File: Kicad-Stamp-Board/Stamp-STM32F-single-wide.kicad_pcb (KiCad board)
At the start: 2 copper layers, 70 x 84 mm, 70 parts, among them J1 +3.3V, J2 GND, J3 Serial, J4 BOOT1, SW1 Reset, SW2 BOOT, U1 STM32Fxxx, U2 ICL3221, Y1 32.768KHz

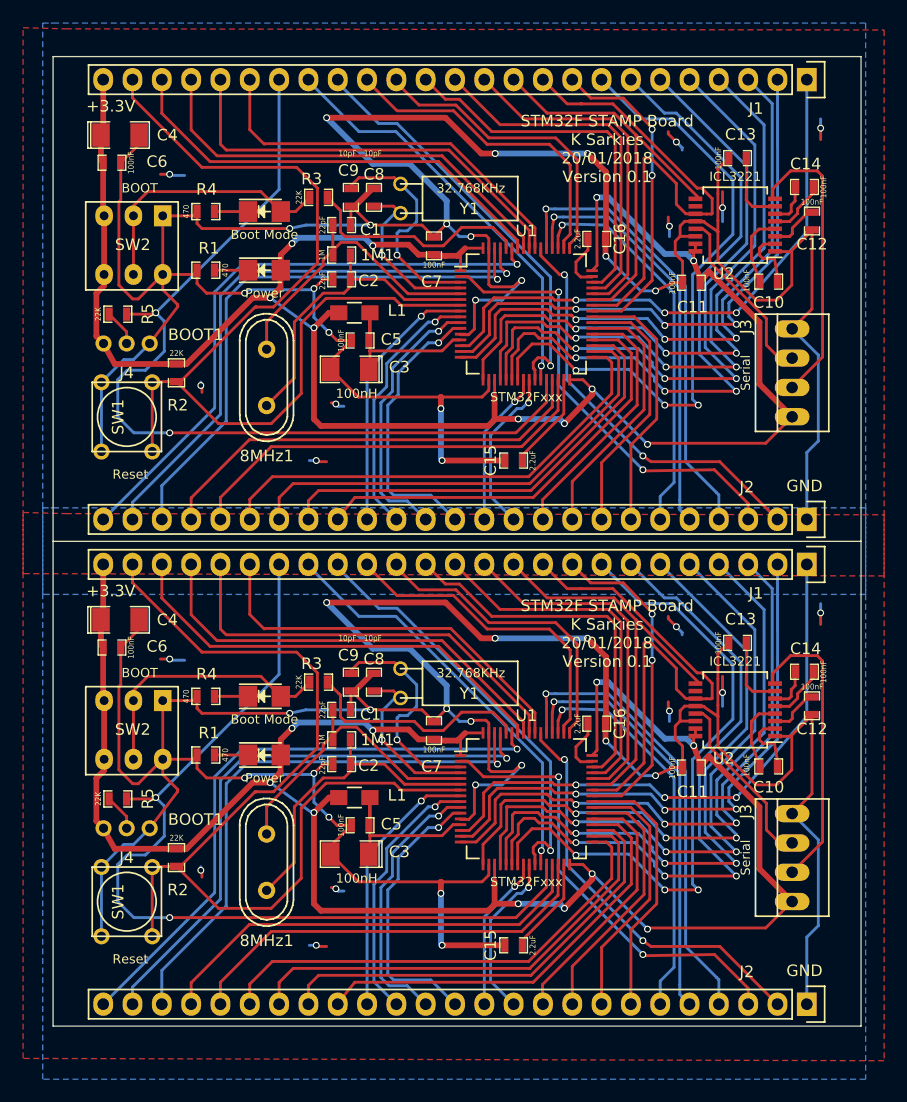
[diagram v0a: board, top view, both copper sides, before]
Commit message: Update PCB to stitch grounds a bit more. Update silk screen. Increase length of PCB to 70mm to satisfy fab house requirements.
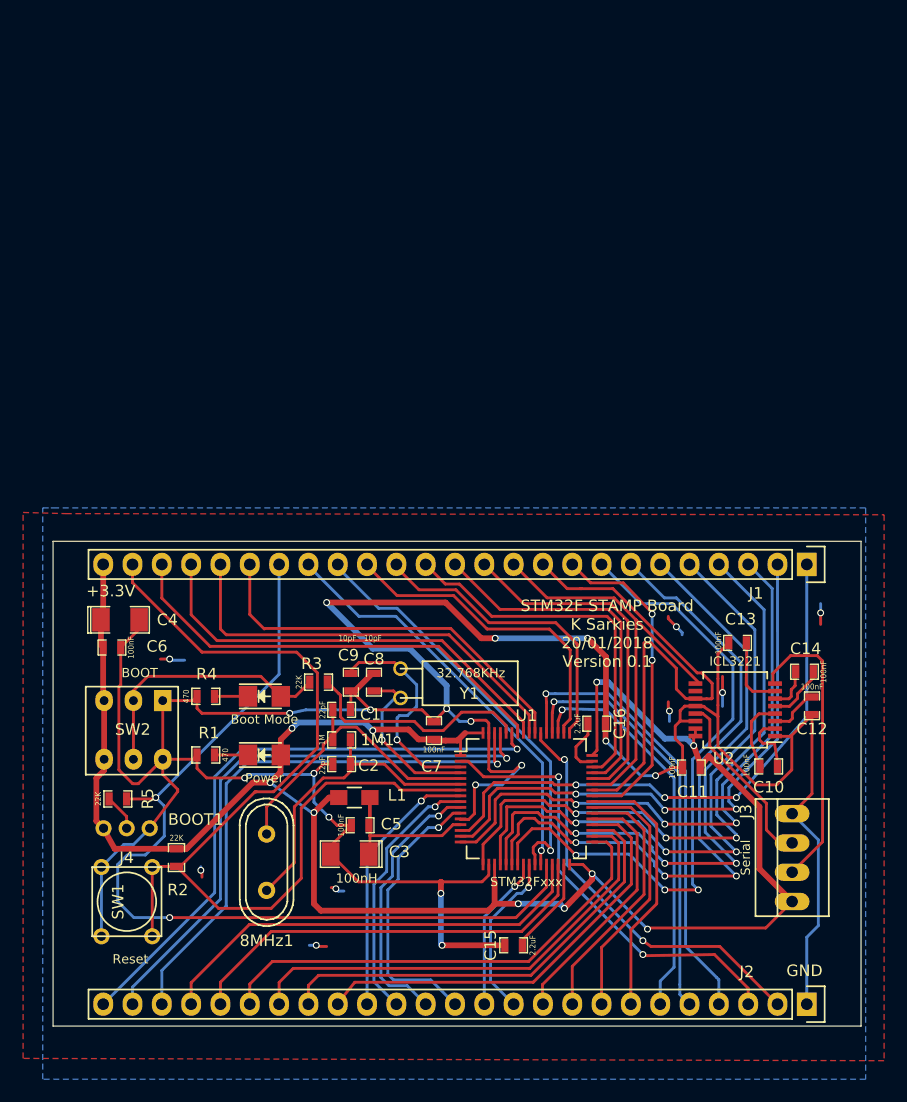
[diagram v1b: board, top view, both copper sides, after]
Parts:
- removed the 1M1 at (137.5, 49.4)
- removed the 8MHz1 at (131.0, 60.0)
- removed the C1 at (137.5, 46.8)
- removed the C10 at (174.5, 51.7)
- removed the C11 at (167.8, 51.8)
- removed the C12 at (178.2, 46.5)
- removed the C13 at (171.8, 41.0)
- removed the C14 at (177.6, 43.5)
- removed the C15 at (152.4, 67.2)
- removed the C16 at (159.6, 48.0)
- removed the C2 at (137.5, 51.5)
- removed the C3 at (138.2, 59.3)
- removed the C4 at (118.3, 39.0)
- removed the C5 at (139.1, 56.8)
- removed the C6 at (117.6, 41.4)
- removed the C7 at (145.5, 48.6)
- removed the C8 at (140.3, 44.4)
- removed the C9 at (138.3, 44.4)
- removed the D1 at (130.8, 50.7)
- removed the D2 at (130.8, 45.6)
- removed the J1 at (177.8, 34.2)
- removed the J2 at (177.8, 72.3)
- removed the J3 at (176.5, 59.6)
- removed the J4 at (118.9, 57.1)
- removed the L1 at (138.6, 54.4)
- removed the R1 at (125.7, 50.7)
- removed the R2 at (123.2, 59.6)
- removed the R3 at (135.5, 44.4)
- removed the R4 at (125.7, 45.6)
- removed the R5 at (118.1, 54.5)
- removed the SW1 at (118.9, 63.4)
- removed the SW2 at (122.0, 46.0)
- removed the U1 at (153.5, 54.5)
- removed the U2 at (171.6, 46.8)
- removed the Y1 at (142.6, 44.5)
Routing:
- net Earth: track 544.9 -> 272.4 mm, vias 32 -> 16
- net 3.3V: track 344.4 -> 172.2 mm, vias 20 -> 10
- net RESET: track 172.7 -> 86.4 mm
- net PB2: track 159.9 -> 79.9 mm, vias 4 -> 2
- net PA6: track 118.9 -> 59.5 mm, vias 6 -> 3
- net PA5: track 115.8 -> 57.9 mm, vias 6 -> 3
- net PA4: track 113.5 -> 56.8 mm, vias 6 -> 3
- net PA7: track 112.9 -> 56.4 mm, vias 6 -> 3
- net PA3: track 111.5 -> 55.7 mm, vias 6 -> 3
- net PA2: track 107.7 -> 53.8 mm, vias 6 -> 3
- net PB7: track 105.2 -> 52.6 mm, vias 2 -> 1
- net PA1: track 102.0 -> 51.0 mm, vias 6 -> 3
- net PB8: track 101.5 -> 50.7 mm, vias 2 -> 1
- net PA0: track 99.7 -> 49.9 mm, vias 6 -> 3
- net PB9: track 97.2 -> 48.6 mm, vias 2 -> 1
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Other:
- board size 70 x 84 mm -> 70 x 42 mm
